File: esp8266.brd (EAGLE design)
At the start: 29.5 x 28.6 mm, 35 parts, among them IC1 74LVC1G08DBV, U1 FT232RL-BASICSSOP, U2 SPX3819M5-L33

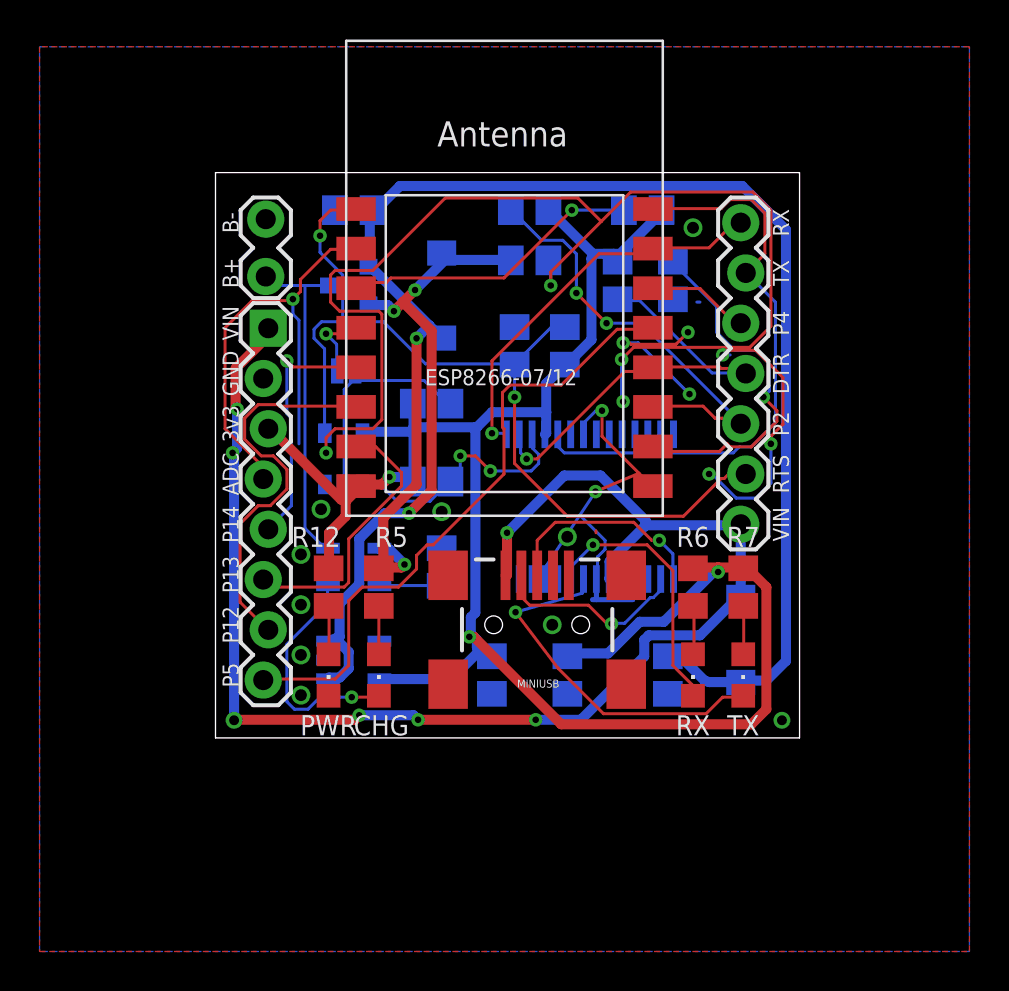
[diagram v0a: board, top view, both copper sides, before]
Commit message: Improve labeling position
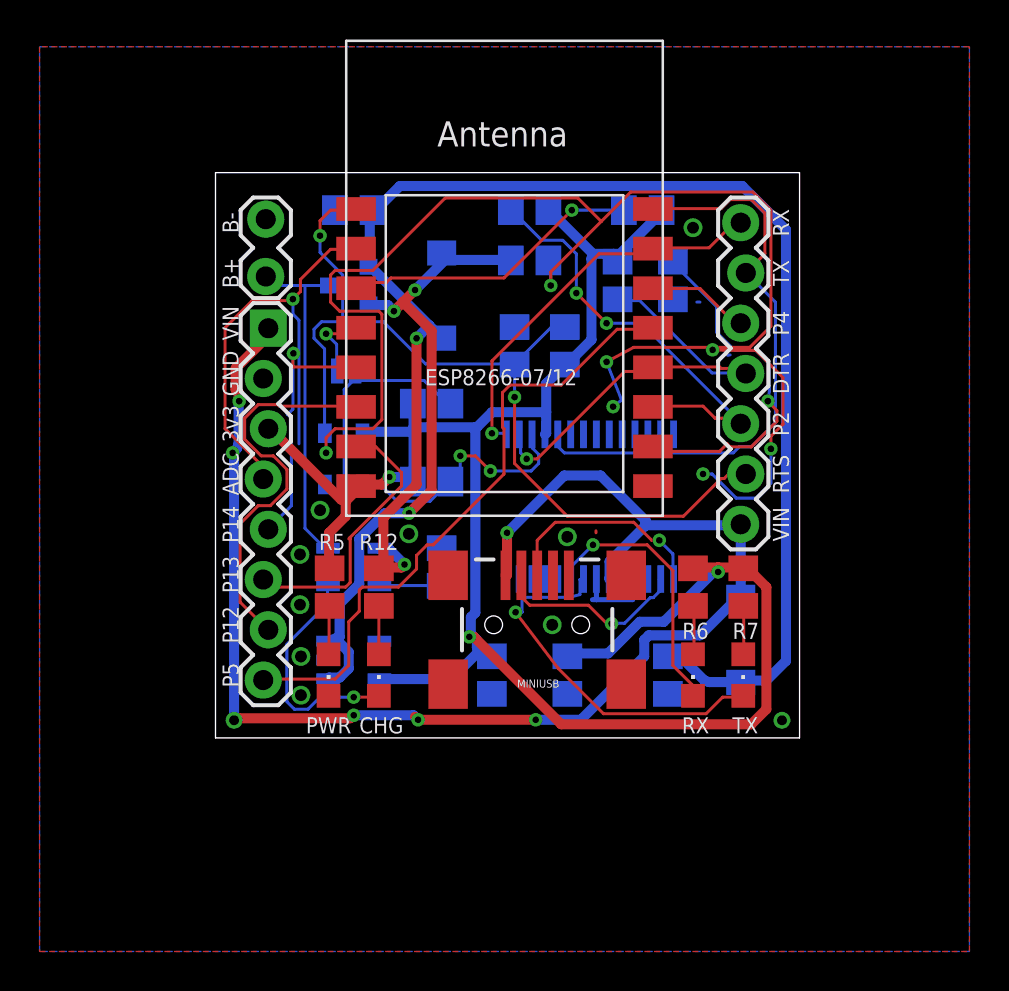
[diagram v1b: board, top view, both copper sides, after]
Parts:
- moved R5 0.05 mm to (14.7, 59.1)
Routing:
- net GND: track 105.3 -> 81.0 mm, vias 22 -> 17
- net P14: track 12.7 -> 13.5 mm
- net RXLED: track 18.5 -> 19.2 mm

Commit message: Add RX and TX probes at the corners and minor style fixes
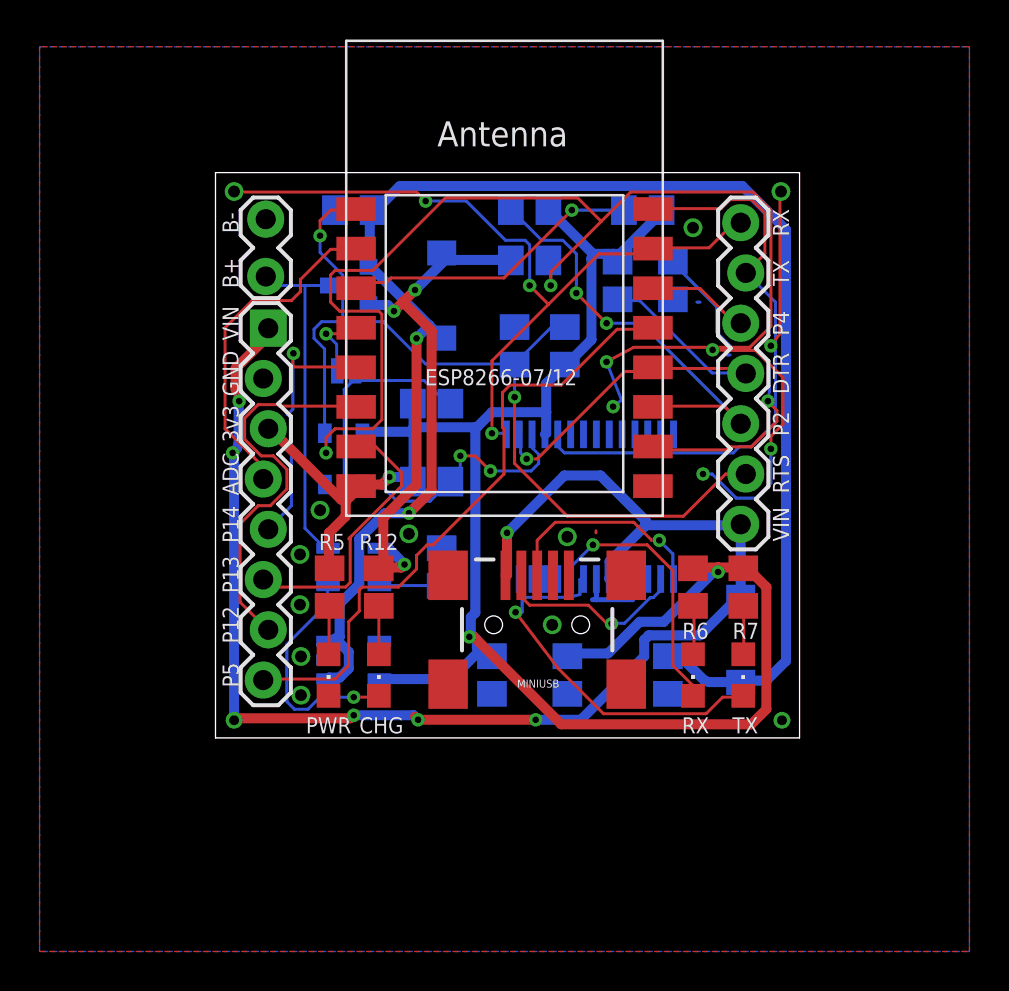
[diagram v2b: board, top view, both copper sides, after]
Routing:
- net RX: track 20.4 -> 39.9 mm, vias 1 -> 4
- net TX: track 30.1 -> 38.4 mm, vias 0 -> 2
- net ADC: track 24.5 -> 17.1 mm, vias 1 -> 0
- net N$5: track 0.00 -> 0.64 mm
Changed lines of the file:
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@@
 <wire x1="35.9664" y1="66.1416" x2="37.2618" y2="67.437" width="0.1524" layer="1"/>
 <wire x1="34.8996" y1="66.1416" x2="35.9664" y2="66.1416" width="0.1524" layer="1"/>
-<wire x1="34.7472" y1="66.294" x2="34.8996" y2="66.1416" width="0.1524" layer="1"/>
-<wire x1="34.3662" y1="65.913" x2="34.7472" y2="66.294" width="0.1524" layer="1"/>
-<wire x1="31.242" y1="65.913" x2="34.3662" y2="65.913" width="0.1524" layer="1"/>
 <wire x1="30.995" y1="66.16" x2="31.242" y2="65.913" width="0.1524" layer="1"/>
 <wire x1="32.004" y1="75.438" x2="32.004" y2="75.499" width="0.1524" layer="16"/>
 <via x="36.8046" y="68.453" extent="1-16" drill="0.3302"/>
+<wire x1="34.7472" y1="65.9892" x2="31.242" y2="65.9892" width="0.1524" layer="1"/>
+<wire x1="34.8996" y1="66.1416" x2="34.7472" y2="65.9892" width="0.1524" layer="1"/>
+<wire x1="31.242" y1="65.9892" x2="30.995" y2="66.16" width="0.1524" layer="1"/>
 </signal>
 <signal name="RX">
@@
 <wire x1="22.86" y1="66.8274" x2="23.5458" y2="66.8274" width="0.1524" layer="16"/>
 <wire x1="22.86" y1="70.485" x2="22.86" y2="66.8274" width="0.1524" layer="1"/>
-<wire x1="28.2702" y1="75.8952" x2="22.86" y2="70.485" width="0.1524" layer="1"/>
+<wire x1="28.2702" y1="75.8952" x2="25.7175" y2="73.3425" width="0.1524" layer="1"/>
+<wire x1="25.7175" y1="73.3425" x2="22.86" y2="70.485" width="0.1524" layer="1"/>
 <wire x1="30.7086" y1="75.8952" x2="28.2702" y2="75.8952" width="0.1524" layer="1"/>
 <wire x1="30.9372" y1="76.1238" x2="30.7086" y2="75.8952" width="0.1524" layer="1"/>
@@
 <wire x1="35.433" y1="77.4192" x2="35.433" y2="77.47" width="0.1524" layer="1"/>
 <wire x1="31.242" y1="76.3524" x2="30.995" y2="76.16" width="0.1524" layer="1"/>
+<via x="9.8298" y="79.0448" extent="1-16" drill="0.6"/>
+<wire x1="19.05" y1="79.0194" x2="9.8298" y2="79.0194" width="0.1524" layer="1"/>
+<wire x1="19.5072" y1="78.5622" x2="19.05" y2="79.0194" width="0.1524" layer="1"/>
+<wire x1="21.5646" y1="78.5622" x2="19.5072" y2="78.5622" width="0.1524" layer="16"/>
+<wire x1="23.5458" y1="76.581" x2="21.5646" y2="78.5622" width="0.1524" layer="16"/>
+<wire x1="24.5364" y1="76.581" x2="23.5458" y2="76.581" width="0.1524" layer="16"/>
+<wire x1="24.765" y1="76.3524" x2="24.5364" y2="76.581" width="0.1524" layer="16"/>
+<wire x1="24.765" y1="74.295" x2="24.765" y2="76.3524" width="0.1524" layer="16"/>
+<wire x1="25.7175" y1="73.3425" x2="24.765" y2="74.295" width="0.1524" layer="1"/>
+<wire x1="9.8298" y1="79.0194" x2="9.8298" y2="79.0448" width="0.1524" layer="1"/>
+<via x="19.5072" y="78.5622" extent="1-16" drill="0.3302"/>
+<via x="24.765" y="74.295" extent="1-16" drill="0.3302"/>
 </signal>
 <signal name="TX">
@@
 <wire x1="35.9664" y1="66.1416" x2="35.3568" y2="66.1416" width="0.1524" layer="16"/>
 <wire x1="37.1856" y1="67.3608" x2="35.9664" y2="66.1416" width="0.1524" layer="16"/>
-<wire x1="37.1856" y1="73.4568" x2="37.1856" y2="67.3608" width="0.1524" layer="16"/>
+<wire x1="37.1856" y1="73.4568" x2="37.1856" y2="71.3994" width="0.1524" layer="16"/>
+<wire x1="37.1856" y1="71.3994" x2="37.1856" y2="67.3608" width="0.1524" layer="16"/>
 <wire x1="26.2128" y1="66.7512" x2="26.188" y2="66.775" width="0.1524" layer="16"/>
 <wire x1="34.4424" y1="78.1812" x2="31.0134" y2="78.1812" width="0.1524" layer="1"/>
@@
 <wire x1="37.1856" y1="73.4568" x2="35.7378" y2="74.9046" width="0.1524" layer="16"/>
 <wire x1="35.7378" y1="74.9046" x2="35.687" y2="74.93" width="0.1524" layer="16"/>
+<via x="37.465" y="79.0448" extent="1-16" drill="0.6"/>
+<wire x1="37.4142" y1="71.8566" x2="37.4142" y2="79.0194" width="0.1524" layer="1"/>
+<wire x1="36.957" y1="71.247" x2="37.4142" y2="71.8566" width="0.1524" layer="1"/>
+<wire x1="37.1856" y1="71.3994" x2="36.957" y2="71.247" width="0.1524" layer="16"/>
+<wire x1="37.4142" y1="79.0194" x2="37.465" y2="79.0448" width="0.1524" layer="1"/>
+<via x="36.957" y="71.247" extent="1-16" drill="0.3302"/>
 </signal>
 <signal name="P14">
@@
 <wire x1="23.8506" y1="78.105" x2="23.815" y2="78.105" width="0.1524" layer="16"/>
 <wire x1="35.433" y1="67.3608" x2="35.433" y2="67.31" width="0.1524" layer="16"/>
-<wire x1="33.528" y1="68.199" x2="31.0134" y2="68.199" width="0.1524" layer="1"/>
-<wire x1="34.1376" y1="67.5894" x2="33.528" y2="68.199" width="0.1524" layer="1"/>
-<wire x1="34.5186" y1="67.5894" x2="34.1376" y2="67.5894" width="0.1524" layer="1"/>
-<wire x1="34.7472" y1="67.3608" x2="34.5186" y2="67.5894" width="0.1524" layer="1"/>
-<wire x1="35.433" y1="67.3608" x2="34.7472" y2="67.3608" width="0.1524" layer="1"/>
+<wire x1="34.5948" y1="68.199" x2="31.0134" y2="68.199" width="0.1524" layer="1"/>
 <wire x1="31.0134" y1="68.199" x2="30.995" y2="68.16" width="0.1524" layer="1"/>
-<wire x1="35.433" y1="67.3608" x2="35.433" y2="67.31" width="0.1524" layer="1"/>
 <via x="27.1272" y="73.914" extent="1-16" drill="0.3302"/>
 <via x="28.6512" y="72.39" extent="1-16" drill="0.3302"/>
+<wire x1="35.433" y1="67.3608" x2="34.5948" y2="68.199" width="0.1524" layer="1"/>
+<wire x1="35.433" y1="67.3608" x2="35.433" y2="67.31" width="0.1524" layer="1"/>
 </signal>
 <signal name="ADC">
@@
 <wire x1="13.1826" y1="74.5998" x2="14.7066" y2="76.1238" width="0.1524" layer="1"/>
 <wire x1="13.1826" y1="73.9902" x2="13.1826" y2="74.5998" width="0.1524" layer="1"/>
-<wire x1="12.8016" y1="73.6092" x2="13.1826" y2="73.9902" width="0.1524" layer="1"/>
-<wire x1="12.8016" y1="72.8472" x2="12.8016" y2="73.6092" width="0.1524" layer="16"/>
-<wire x1="13.1064" y1="72.5424" x2="12.8016" y2="72.8472" width="0.1524" layer="16"/>
-<wire x1="13.1064" y1="66.294" x2="13.1064" y2="72.5424" width="0.1524" layer="16"/>
+<wire x1="12.7254" y1="73.533" x2="13.1826" y2="73.9902" width="0.1524" layer="1"/>
 <wire x1="15.9258" y1="76.1238" x2="15.995" y2="76.16" width="0.1524" layer="1"/>
-<via x="12.8016" y="73.6092" extent="1-16" drill="0.3302"/>
 <contactref element="JP1" pad="4"/>
 <wire x1="11.2776" y1="65.151" x2="11.2776" y2="64.5414" width="0.1524" layer="1"/>
@@
 <wire x1="10.7442" y1="73.533" x2="9.3726" y2="72.1614" width="0.1524" layer="1"/>
 <wire x1="12.7254" y1="73.533" x2="10.7442" y2="73.533" width="0.1524" layer="1"/>
-<wire x1="12.8016" y1="73.6092" x2="12.7254" y2="73.533" width="0.1524" layer="1"/>
 <wire x1="11.2776" y1="64.5414" x2="11.303" y2="64.516" width="0.1524" layer="1"/>
 </signal>
@@
 <wire x1="29.2608" y1="73.533" x2="29.21" y2="73.599" width="0.1524" layer="16"/>
 <wire x1="35.6616" y1="69.8754" x2="35.687" y2="69.85" width="0.1524" layer="16"/>
-<wire x1="34.3662" y1="70.1802" x2="31.0134" y2="70.1802" width="0.1524" layer="1"/>
-<wire x1="34.4424" y1="70.104" x2="34.3662" y2="70.1802" width="0.1524" layer="1"/>
-<wire x1="35.433" y1="70.104" x2="34.4424" y2="70.104" width="0.1524" layer="1"/>
-<wire x1="35.687" y1="69.85" x2="35.433" y2="70.104" width="0.1524" layer="1"/>
 <wire x1="31.0134" y1="70.1802" x2="30.995" y2="70.16" width="0.1524" layer="1"/>
 <via x="24.6126" y="65.532" extent="1-16" drill="0.3302"/>
+<wire x1="34.8234" y1="70.104" x2="31.0134" y2="70.104" width="0.1524" layer="1"/>
+<wire x1="31.0134" y1="70.104" x2="30.995" y2="70.16" width="0.1524" layer="1"/>
+<wire x1="35.052" y1="69.8754" x2="35.6616" y2="69.8754" width="0.1524" layer="1"/>
+<wire x1="34.8234" y1="70.104" x2="35.052" y2="69.8754" width="0.1524" layer="1"/>
+<wire x1="35.6616" y1="69.8754" x2="35.687" y2="69.85" width="0.1524" layer="1"/>
 </signal>
 <signal name="RTS">
@@
 <wire x1="15.3162" y1="72.4662" x2="15.3162" y2="74.8284" width="0.1524" layer="16"/>
 <wire x1="15.9258" y1="78.105" x2="15.995" y2="78.16" width="0.1524" layer="1"/>
-<wire x1="34.8234" y1="64.77" x2="35.687" y2="64.77" width="0.1524" layer="1"/>
-<wire x1="34.5948" y1="64.5414" x2="34.8234" y2="64.77" width="0.1524" layer="1"/>
-<wire x1="34.4424" y1="64.5414" x2="34.5948" y2="64.5414" width="0.1524" layer="1"/>
-<wire x1="32.5374" y1="62.6364" x2="34.4424" y2="64.5414" width="0.1524" layer="1"/>
+<wire x1="32.5374" y1="62.6364" x2="34.671" y2="64.77" width="0.1524" layer="1"/>
 <wire x1="26.67" y1="62.6364" x2="32.5374" y2="62.6364" width="0.1524" layer="1"/>
 <wire x1="24.003" y1="65.3034" x2="26.67" y2="62.6364" width="0.1524" layer="1"/>
@@
 <via x="14.1732" y="76.8096" extent="1-16" drill="0.3302"/>
 <via x="24.003" y="68.6562" extent="1-16" drill="0.3302"/>
+<wire x1="34.671" y1="64.77" x2="35.687" y2="64.77" width="0.1524" layer="1"/>
 </signal>
 <signal name="VRIN" class="1">
@@
 <wire x1="15.9258" y1="69.4944" x2="15.944" y2="69.977" width="0.1524" layer="16"/>
 </signal>
+<signal name="N$5">
+<wire x1="31.75" y1="70.485" x2="31.75" y2="69.85" width="0.1524" layer="1"/>
+</signal>
 </signals>

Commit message: Added OSHPark design rules Fixed half a dozen design rules violations (overlapping and clearance).
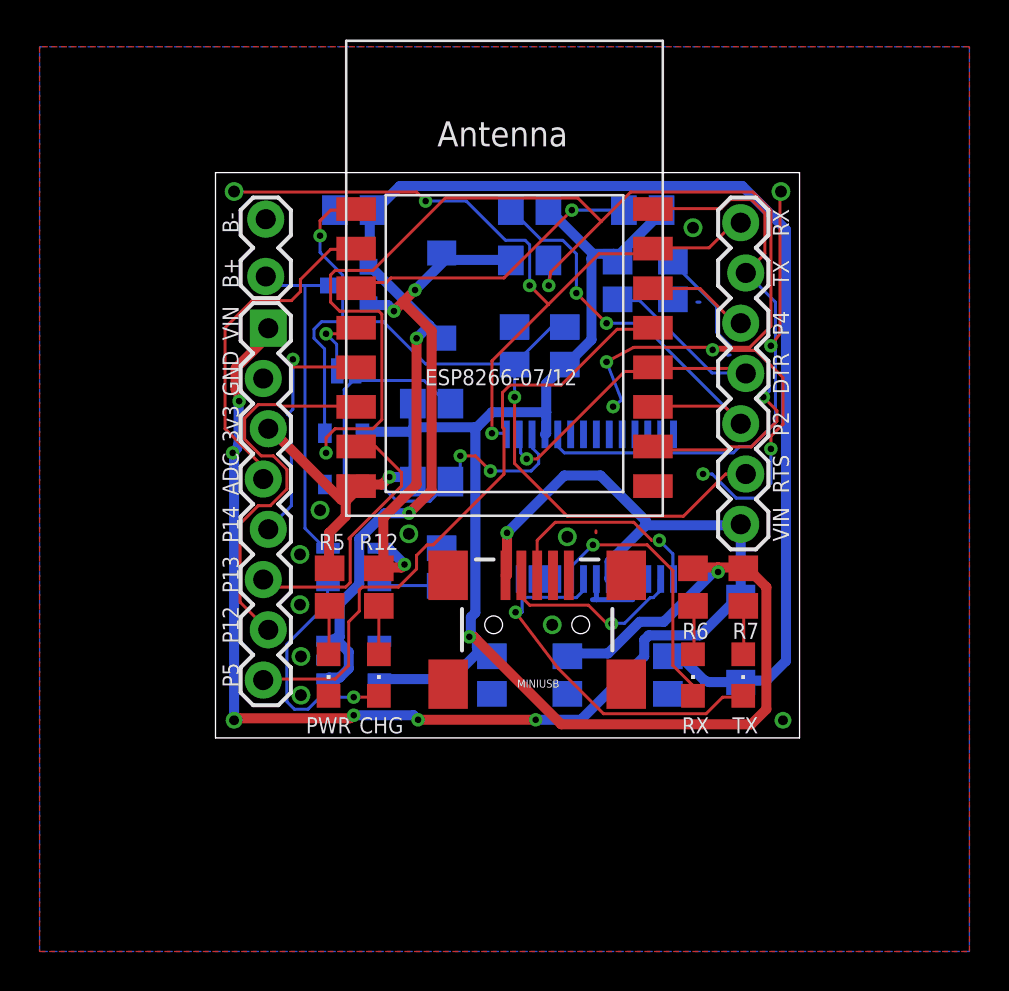
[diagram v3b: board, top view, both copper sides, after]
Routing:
- net P14: track 13.5 -> 12.9 mm
- net N$5: track 0.64 -> 0.00 mm

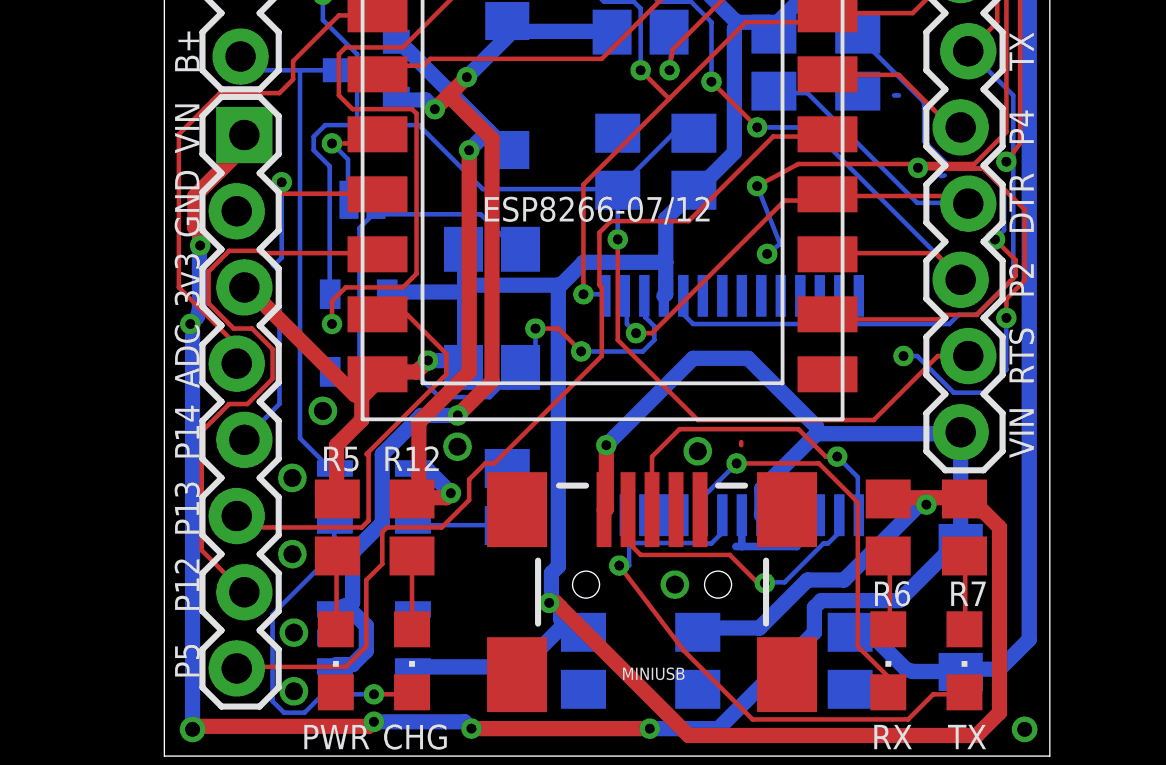
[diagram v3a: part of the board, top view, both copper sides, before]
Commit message: Optimised the layout: deleted several redundant wires and at least one via.
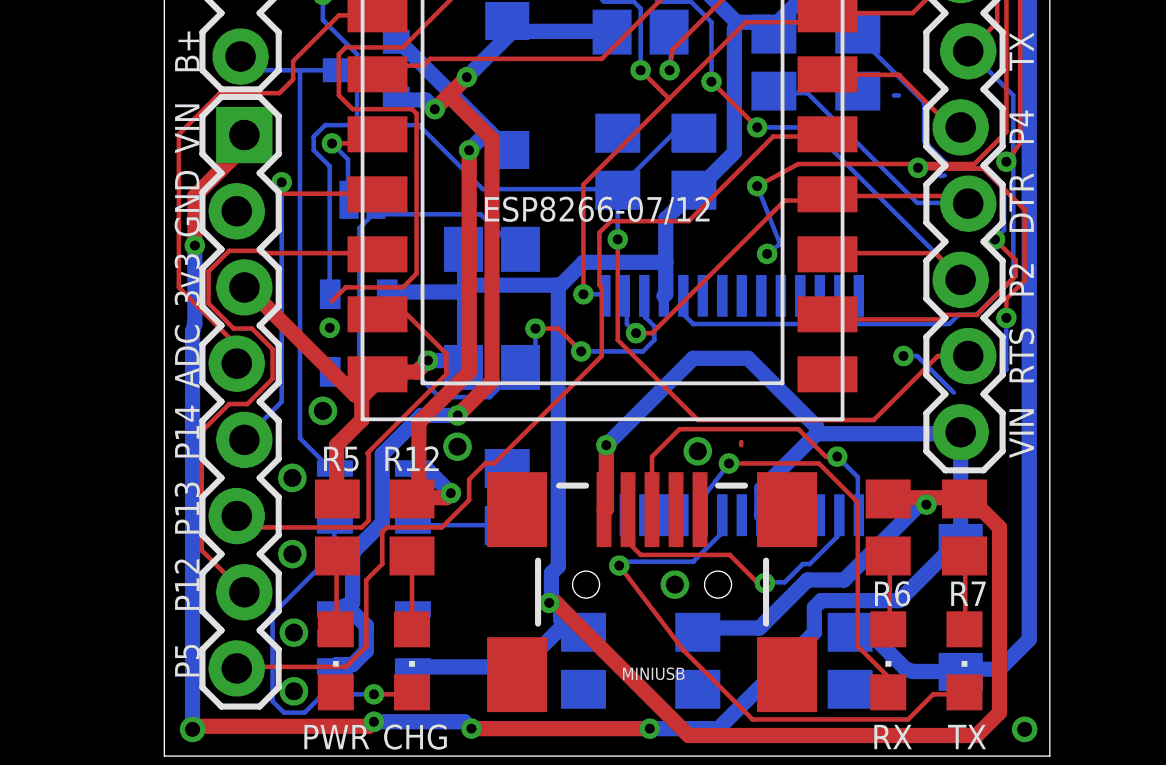
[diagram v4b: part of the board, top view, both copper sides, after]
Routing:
- net GND: track 81.1 -> 75.1 mm
- net VIN: track 73.1 -> 73.0 mm, vias 7 -> 6
